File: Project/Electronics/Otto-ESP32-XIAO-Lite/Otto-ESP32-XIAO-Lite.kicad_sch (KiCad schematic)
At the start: 22 parts, among them J1 Conn_01x03, J10 Conn_01x02, J12 OLED 0,91" - I2C (SKU21796), J13 MPU6050, J2 Conn_01x03, J3 Conn_01x03, J4 Conn_01x03, J5 Conn_01x03, J6 Conn_01x03, J7 Conn_01x04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

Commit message: add qrCode - clean PCB
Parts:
- removed JP1: SolderJumper_3_Open, Jumper:SolderJumper-3_P2.0mm_Open_TrianglePad1.0x1.5mm_NumberLabels, symbol Jumper:SolderJumper_3_Open
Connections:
- net +5V: now also J5.2 (Pin_2), J6.2 (Pin_2)
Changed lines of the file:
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@@
 	(wire
 		(pts
-			(xy 215.9 104.14) (xy 215.9 101.6)
+			(xy 215.9 99.06) (xy 215.9 104.14)
 		)
 		(stroke
@@
 	)
 	(symbol
-		(lib_id "Jumper:SolderJumper_3_Open")
-		(at 215.9 97.79 0)
-		(unit 1)
-		(exclude_from_sim yes)
-		(in_bom no)
-		(on_board yes)
-		(dnp no)
-		(fields_autoplaced yes)
-		(property "Reference" "JP1"
-			(at 215.9 91.44 0)
-			(effects
-				(font
-					(size 1.27 1.27)
-				)
-			)
-		)
-		(property "Value" "SolderJumper_3_Open"
-			(at 215.9 93.98 0)
-			(effects
-				(font
-					(size 1.27 1.27)
-				)
-			)
-		)
-		(property "Footprint" "Jumper:SolderJumper-3_P2.0mm_Open_TrianglePad1.0x1.5mm_NumberLabels"
-			(at 215.9 97.79 0)
-			(effects
-				(font
-					(size 1.27 1.27)
-				)
-				(hide yes)
-			)
-		)
-		(property "Datasheet" "~"
-			(at 215.9 97.79 0)
-			(effects
-				(font
-					(size 1.27 1.27)
-				)
-				(hide yes)
-			)
-		)
-		(property "Description" "Solder Jumper, 3-pole, open"
-			(at 215.9 97.79 0)
-			(effects
-				(font
-					(size 1.27 1.27)
-				)
-				(hide yes)
-			)
-		)
-		(pin "1"
-		)
-		(pin "2"
-		)
-		(pin "3"
-		)
-		(instances
-			(project ""
-				(path "/d2682c99-4285-4c0b-9e61-08b763b3ce0d"
-					(reference "JP1")
-					(unit 1)
-				)
-			)
-		)
-	)
-	(symbol
 		(lib_id "power:+3.3V")
 		(at 58.42 111.76 270)
@@
 	(symbol
 		(lib_id "power:+5V")
-		(at 210.82 97.79 90)
+		(at 215.9 99.06 0)
 		(unit 1)
 		(exclude_from_sim no)
@@
 		(fields_autoplaced yes)
 		(property "Reference" "#PWR018"
-			(at 214.63 97.79 0)
+			(at 215.9 102.87 0)
 			(effects
 				(font
@@
 		)
 		(property "Value" "+5V"
-			(at 207.01 97.7899 90)
+			(at 218.44 97.7899 0)
 			(effects
 				(font
@@
 		)
 		(property "Footprint" ""
-			(at 210.82 97.79 0)
+			(at 215.9 99.06 0)
 			(effects
 				(font
@@
 		)
 		(property "Datasheet" ""
-			(at 210.82 97.79 0)
+			(at 215.9 99.06 0)
 			(effects
 				(font
@@
 		)
 		(property "Description" "Power symbol creates a global label with name \"+5V\""
-			(at 210.82 97.79 0)
+			(at 215.9 99.06 0)
 			(effects
 				(font
@@
 					(unit 1)
 				)
-			)
-		)
-	)
-	(symbol
-		(lib_id "power:+3.3V")
-		(at 220.98 97.79 270)
-		(unit 1)
-		(exclude_from_sim no)
-		(in_bom yes)
-		(on_board yes)
-		(dnp no)
-		(fields_autoplaced yes)
-		(property "Reference" "#PWR020"
-			(at 217.17 97.79 0)
-			(effects
-				(font
-					(size 1.27 1.27)
-				)
-				(hide yes)
-			)
-		)
-		(property "Value" "+3.3V"
-			(at 224.79 97.7899 90)
-			(effects
-				(font
-					(size 1.27 1.27)
-				)
-				(justify left)
-			)
-		)
-		(property "Footprint" ""
-			(at 220.98 97.79 0)
-			(effects
-				(font
-					(size 1.27 1.27)
-				)
-				(hide yes)
-			)
-		)
-		(property "Datasheet" ""
-			(at 220.98 97.79 0)
-			(effects
-				(font
-					(size 1.27 1.27)
-				)
-				(hide yes)
-			)
-		)
-		(property "Description" "Power symbol creates a global label with name \"+3.3V\""
-			(at 220.98 97.79 0)
-			(effects
-				(font
-					(size 1.27 1.27)
-				)
-				(hide yes)
-			)
-		)
-		(pin "1"
-		)
-		(instances
-			(project "CarteDummy"
-				(path "/d2682c99-4285-4c0b-9e61-08b763b3ce0d"
-					(reference "#PWR020")
-					(unit 1)
-				)

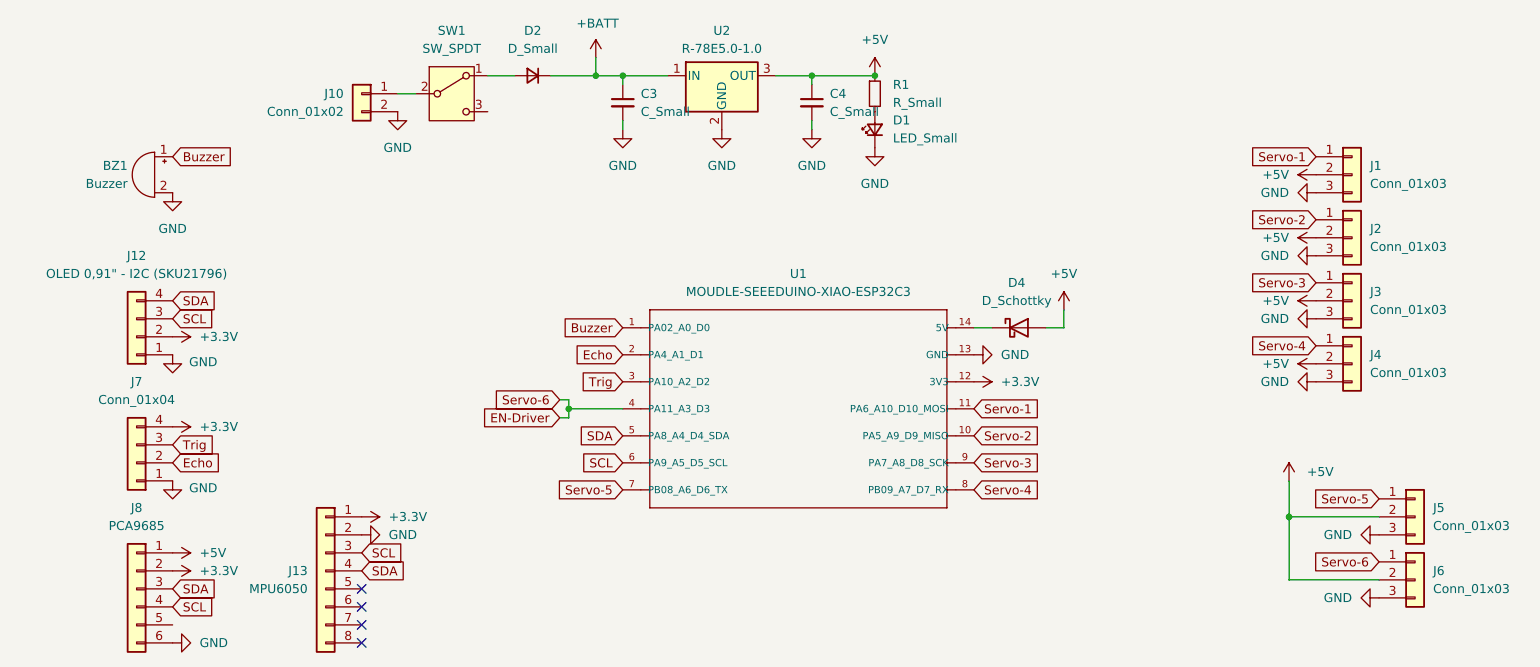
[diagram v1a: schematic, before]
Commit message: Clean up the Schematic
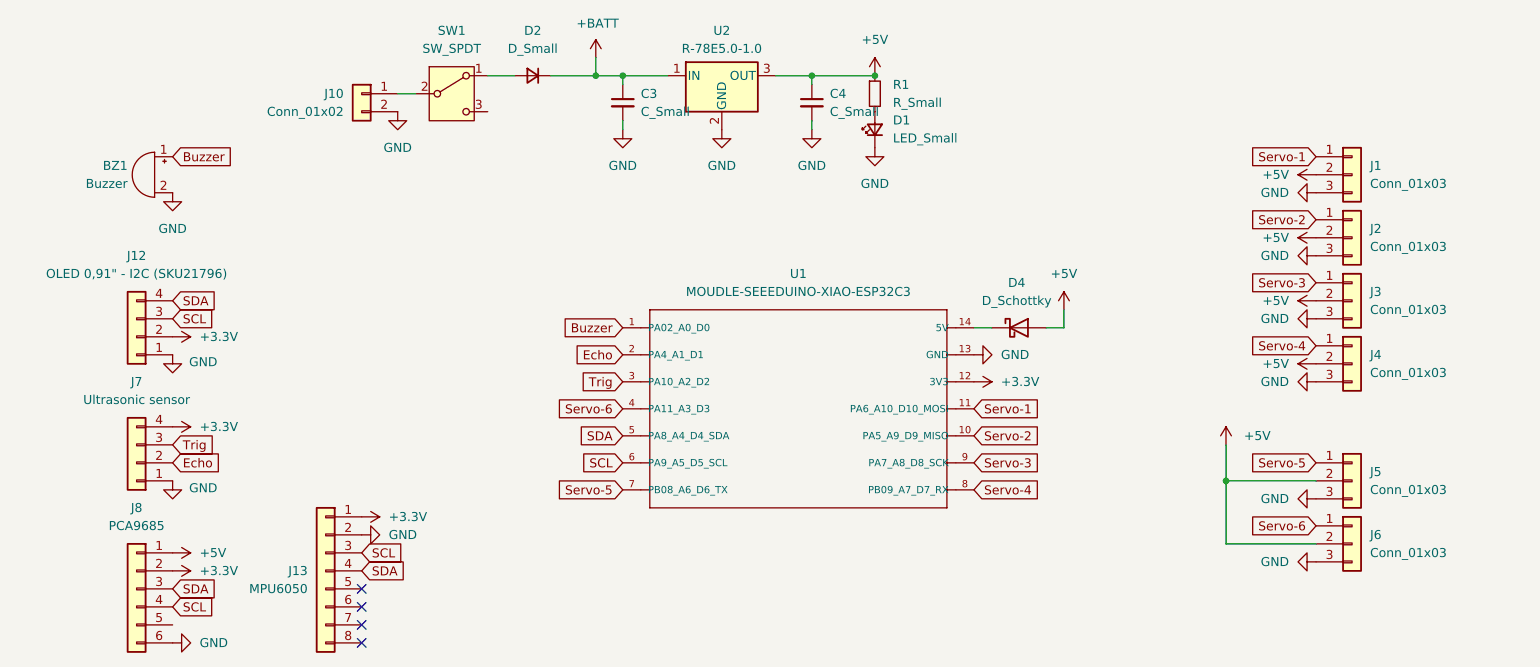
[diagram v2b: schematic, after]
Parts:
- J7: value Conn_01x04 -> Ultrasonic sensor
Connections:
- net EN-Driver renamed Servo-6
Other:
- moved on the sheet: J5, J6
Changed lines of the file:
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@@
 	(paper "A4")
 	(junction
-		(at 114.3 88.9)
-		(diameter 0)
-		(color 0 0 0 0)
-	)
-	(junction
 		(at 121.92 41.91)
 		(diameter 0)
@@
 	)
 	(junction
-		(at 215.9 104.14)
+		(at 207.01 99.06)
 		(diameter 0)
 		(color 0 0 0 0)
@@
 	(wire
 		(pts
-			(xy 228.6 104.14) (xy 215.9 104.14)
-		)
-		(stroke
-			(width 0)
-			(type default)
-		)
-	)
-	(wire
-		(pts
-			(xy 228.6 113.03) (xy 215.9 113.03)
+			(xy 219.71 99.06) (xy 207.01 99.06)
 		)
 		(stroke
@@
 	(wire
 		(pts
-			(xy 114.3 88.9) (xy 121.92 88.9)
+			(xy 219.71 107.95) (xy 207.01 107.95)
 		)
 		(stroke
@@
 	(wire
 		(pts
-			(xy 114.3 87.63) (xy 114.3 88.9)
-		)
-		(stroke
-			(width 0)
-			(type default)
-		)
-	)
-	(wire
-		(pts
 			(xy 102.87 41.91) (xy 106.68 41.91)
 		)
@@
 	(wire
 		(pts
-			(xy 113.03 90.17) (xy 114.3 90.17)
-		)
-		(stroke
-			(width 0)
-			(type default)
-		)
-	)
-	(wire
-		(pts
-			(xy 215.9 99.06) (xy 215.9 104.14)
-		)
-		(stroke
-			(width 0)
-			(type default)
-		)
-	)
-	(wire
-		(pts
-			(xy 113.03 87.63) (xy 114.3 87.63)
+			(xy 207.01 93.98) (xy 207.01 99.06)
 		)
 		(stroke
@@
 	(wire
 		(pts
-			(xy 114.3 88.9) (xy 114.3 90.17)
-		)
-		(stroke
-			(width 0)
-			(type default)
-		)
-	)
-	(wire
-		(pts
-			(xy 215.9 113.03) (xy 215.9 104.14)
+			(xy 207.01 107.95) (xy 207.01 99.06)
 		)
 		(stroke
@@
 	(global_label "Servo-6"
 		(shape input)
-		(at 113.03 87.63 180)
+		(at 121.92 88.9 180)
 		(fields_autoplaced yes)
 		(effects
@@
 		)
 		(property "Intersheetrefs" "${INTERSHEET_REFS}"
-			(at 102.062 87.63 0)
+			(at 110.952 88.9 0)
 			(effects
 				(font
@@
 		)
 	)
-	(global_label "EN-Driver"
-		(shape input)
-		(at 113.03 90.17 180)
-		(fields_autoplaced yes)
-		(effects
-			(font
-				(size 1.27 1.27)
-			)
-			(justify right)
-		)
-		(property "Intersheetrefs" "${INTERSHEET_REFS}"
-			(at 100.4895 90.17 0)
-			(effects
-				(font
-					(size 1.27 1.27)
-				)
-				(justify right)
-				(hide yes)
-			)
-		)
-	)
 	(global_label "Trig"
 		(shape input)
@@
 	(global_label "Servo-6"
 		(shape input)
-		(at 228.6 110.49 180)
+		(at 219.71 105.41 180)
 		(fields_autoplaced yes)
 		(effects
@@
 		)
 		(property "Intersheetrefs" "${INTERSHEET_REFS}"
-			(at 217.632 110.49 0)
+			(at 208.742 105.41 0)
 			(effects
 				(font
@@
 	(global_label "Servo-5"
 		(shape input)
-		(at 228.6 101.6 180)
+		(at 219.71 96.52 180)
 		(fields_autoplaced yes)
 		(effects
@@
 		)
 		(property "Intersheetrefs" "${INTERSHEET_REFS}"
-			(at 217.632 101.6 0)
+			(at 208.742 96.52 0)
 			(effects
 				(font
@@
 	(symbol
 		(lib_id "Connector_Generic:Conn_01x03")
-		(at 233.68 113.03 0)
+		(at 224.79 107.95 0)
 		(unit 1)
 		(exclude_from_sim no)
@@
 		(fields_autoplaced yes)
 		(property "Reference" "J6"
-			(at 236.22 111.7599 0)
+			(at 227.33 106.6799 0)
 			(effects
 				(font
@@
 		)
 		(property "Value" "Conn_01x03"
-			(at 236.22 114.2999 0)
+			(at 227.33 109.2199 0)
 			(effects
 				(font
@@
 		)
 		(property "Footprint" "Connector_PinHeader_2.54mm:PinHeader_1x03_P2.54mm_Vertical"
-			(at 233.68 113.03 0)
+			(at 224.79 107.95 0)
 			(effects
 				(font
@@
 		)
 		(property "Datasheet" "~"
-			(at 233.68 113.03 0)
+			(at 224.79 107.95 0)
 			(effects
 				(font
@@
 		)
 		(property "Description" "Generic connector, single row, 01x03, script generated (kicad-library-utils/schlib/autogen/connector/)"
-			(at 233.68 113.03 0)
+			(at 224.79 107.95 0)
 			(effects
 				(font
@@
 	(symbol
 		(lib_id "Connector_Generic:Conn_01x03")
-		(at 233.68 104.14 0)
+		(at 224.79 99.06 0)
 		(unit 1)
 		(exclude_from_sim no)
@@
 		(fields_autoplaced yes)
 		(property "Reference" "J5"
-			(at 236.22 102.8699 0)
+			(at 227.33 97.7899 0)
 			(effects
 				(font
@@
 		)
 		(property "Value" "Conn_01x03"
-			(at 236.22 105.4099 0)
+			(at 227.33 100.3299 0)
 			(effects
 				(font
@@
 		)
 		(property "Footprint" "Connector_PinHeader_2.54mm:PinHeader_1x03_P2.54mm_Vertical"
-			(at 233.68 104.14 0)
+			(at 224.79 99.06 0)
 			(effects
 				(font
@@
 		)
 		(property "Datasheet" "~"
-			(at 233.68 104.14 0)
+			(at 224.79 99.06 0)
 			(effects
 				(font
@@
 		)
 		(property "Description" "Generic connector, single row, 01x03, script generated (kicad-library-utils/schlib/autogen/connector/)"
-			(at 233.68 104.14 0)
+			(at 224.79 99.06 0)
 			(effects
 				(font
@@
 	(symbol
 		(lib_id "power:+5V")
-		(at 215.9 99.06 0)
+		(at 207.01 93.98 0)
 		(unit 1)
 		(exclude_from_sim no)
@@
 		(fields_autoplaced yes)
 		(property "Reference" "#PWR018"
-			(at 215.9 102.87 0)
+			(at 207.01 97.79 0)
 			(effects
 				(font
@@
 		)
 		(property "Value" "+5V"
-			(at 218.44 97.7899 0)
+			(at 209.55 92.7099 0)
 			(effects
 				(font
@@
 		)
 		(property "Footprint" ""
-			(at 215.9 99.06 0)
+			(at 207.01 93.98 0)
 			(effects
 				(font
@@
 		)
 		(property "Datasheet" ""
-			(at 215.9 99.06 0)
+			(at 207.01 93.98 0)
 			(effects
 				(font
@@
 		)
 		(property "Description" "Power symbol creates a global label with name \"+5V\""
-			(at 215.9 99.06 0)
+			(at 207.01 93.98 0)
 			(effects
 				(font
@@
 	(symbol
 		(lib_id "power:GND")
-		(at 228.6 115.57 270)
+		(at 219.71 110.49 270)
 		(unit 1)
 		(exclude_from_sim no)
@@
 		(fields_autoplaced yes)
 		(property "Reference" "#PWR021"
-			(at 222.25 115.57 0)
+			(at 213.36 110.49 0)
 			(effects
 				(font
@@
 		)
 		(property "Value" "GND"
-			(at 224.79 115.5699 90)
+			(at 215.9 110.4899 90)
 			(effects
 				(font
@@
 		)
 		(property "Footprint" ""
-			(at 228.6 115.57 0)
+			(at 219.71 110.49 0)
 			(effects
 				(font
@@
 		)
 		(property "Datasheet" ""
-			(at 228.6 115.57 0)
+			(at 219.71 110.49 0)
 			(effects
 				(font
@@
 		)
 		(property "Description" "Power symbol creates a global label with name \"GND\" , ground"
-			(at 228.6 115.57 0)
+			(at 219.71 110.49 0)
 			(effects
 				(font
@@
 			)
 		)
-		(property "Value" "Conn_01x04"
+		(property "Value" "Ultrasonic sensor"
 			(at 53.34 87.63 0)
 			(effects
@@
 	(symbol
 		(lib_id "power:GND")
-		(at 228.6 106.68 270)
+		(at 219.71 101.6 270)
 		(unit 1)
 		(exclude_from_sim no)
@@
 		(fields_autoplaced yes)
 		(property "Reference" "#PWR019"
-			(at 222.25 106.68 0)
+			(at 213.36 101.6 0)
 			(effects
 				(font
@@
 		)
 		(property "Value" "GND"
-			(at 224.79 106.6799 90)
+			(at 215.9 101.5999 90)
 			(effects
 				(font
@@
 		)
 		(property "Footprint" ""
-			(at 228.6 106.68 0)
+			(at 219.71 101.6 0)
 			(effects
 				(font
@@
 		)
 		(property "Datasheet" ""
-			(at 228.6 106.68 0)
+			(at 219.71 101.6 0)
 			(effects
 				(font
@@
 		)
 		(property "Description" "Power symbol creates a global label with name \"GND\" , ground"
-			(at 228.6 106.68 0)
+			(at 219.71 101.6 0)
 			(effects
 				(font
